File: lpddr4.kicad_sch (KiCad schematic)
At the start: 43 parts, among them U1 MT53E1G32D2NP-046

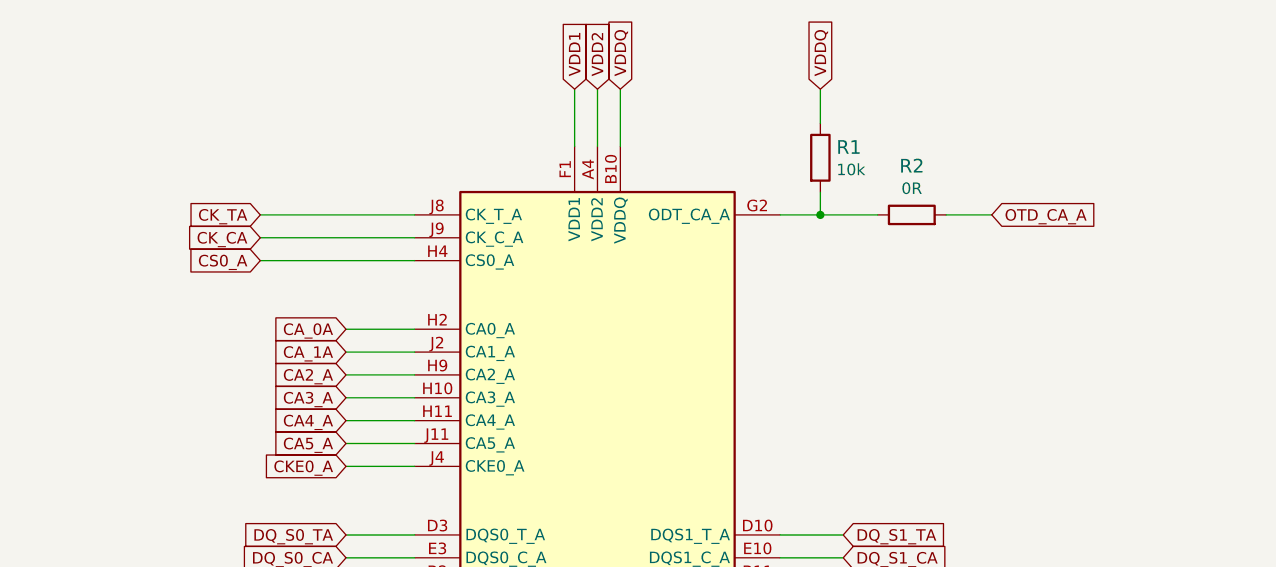
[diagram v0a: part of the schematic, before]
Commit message: Fix net names
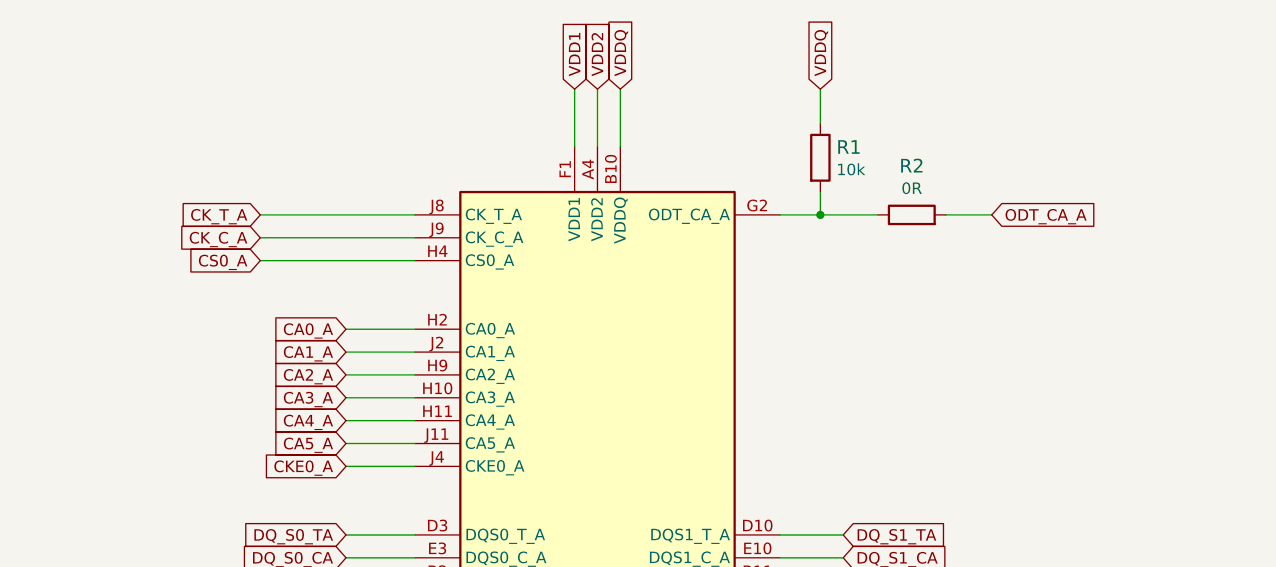
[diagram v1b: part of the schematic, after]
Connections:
- net CA_0A renamed CA0_A
- net CA_1A renamed CA1_A
- net CK_CA renamed CK_C_A
- net CK_TA renamed CK_T_A
- net OTD_CA_A renamed ODT_CA_A

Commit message: Update signage
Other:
- moved on the sheet: C1, C10, C11, C12, C13, C14, C15, C16, C17, C18, C19, C2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

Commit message: [#45231] globlib
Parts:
- C1, C10, C11, C12, C13, C14, C15, C16, C17, C18, C19, C2, C20, C21, C22, C23, C24, C25, C26, C27, C28, C29, C3, C30, C31, C32, C33, C35, C36, C4, C5, C6, C7, C8, C9: footprint lpddr4-testbed-footprints:0201-res -> antmicro-footprints:C_0201; symbol lpddr4-testbed:C_100n_0201 -> antmicroCapacitorsmisc:C_100n_0201
- R1, R3, R4, R5: footprint lpddr4-testbed-footprints:0402-res -> antmicro-footprints:R_0402_1005Metric; symbol lpddr4-testbed:R_10k_0402 -> antmicroResistors0402:R_10k_0402
- R2, R7: footprint lpddr4-testbed-footprints:0402-res -> antmicro-footprints:R_0402_1005Metric; symbol lpddr4-testbed:R_0R_0402 -> antmicroResistors0402:R_0R_0402
- R6: footprint lpddr4-testbed-footprints:0402-res -> antmicro-footprints:R_0402_1005Metric; symbol lpddr4-testbed:R_240R_0402 -> antmicroResistors0402:R_240R_0402
- U1: footprint lpddr4-testbed-footprints:BGA-200_10.0x14.5mm_Layout12x22_P0.80x0.65mm -> antmicro-footprints:BGA-200_10.0x14.5mm_Layout12x22_P0.80x0.65mm; symbol lpddr4-testbed:MT53E1G32D2NP-046 -> antmicroMemory:MT53E1G32D2NP-046

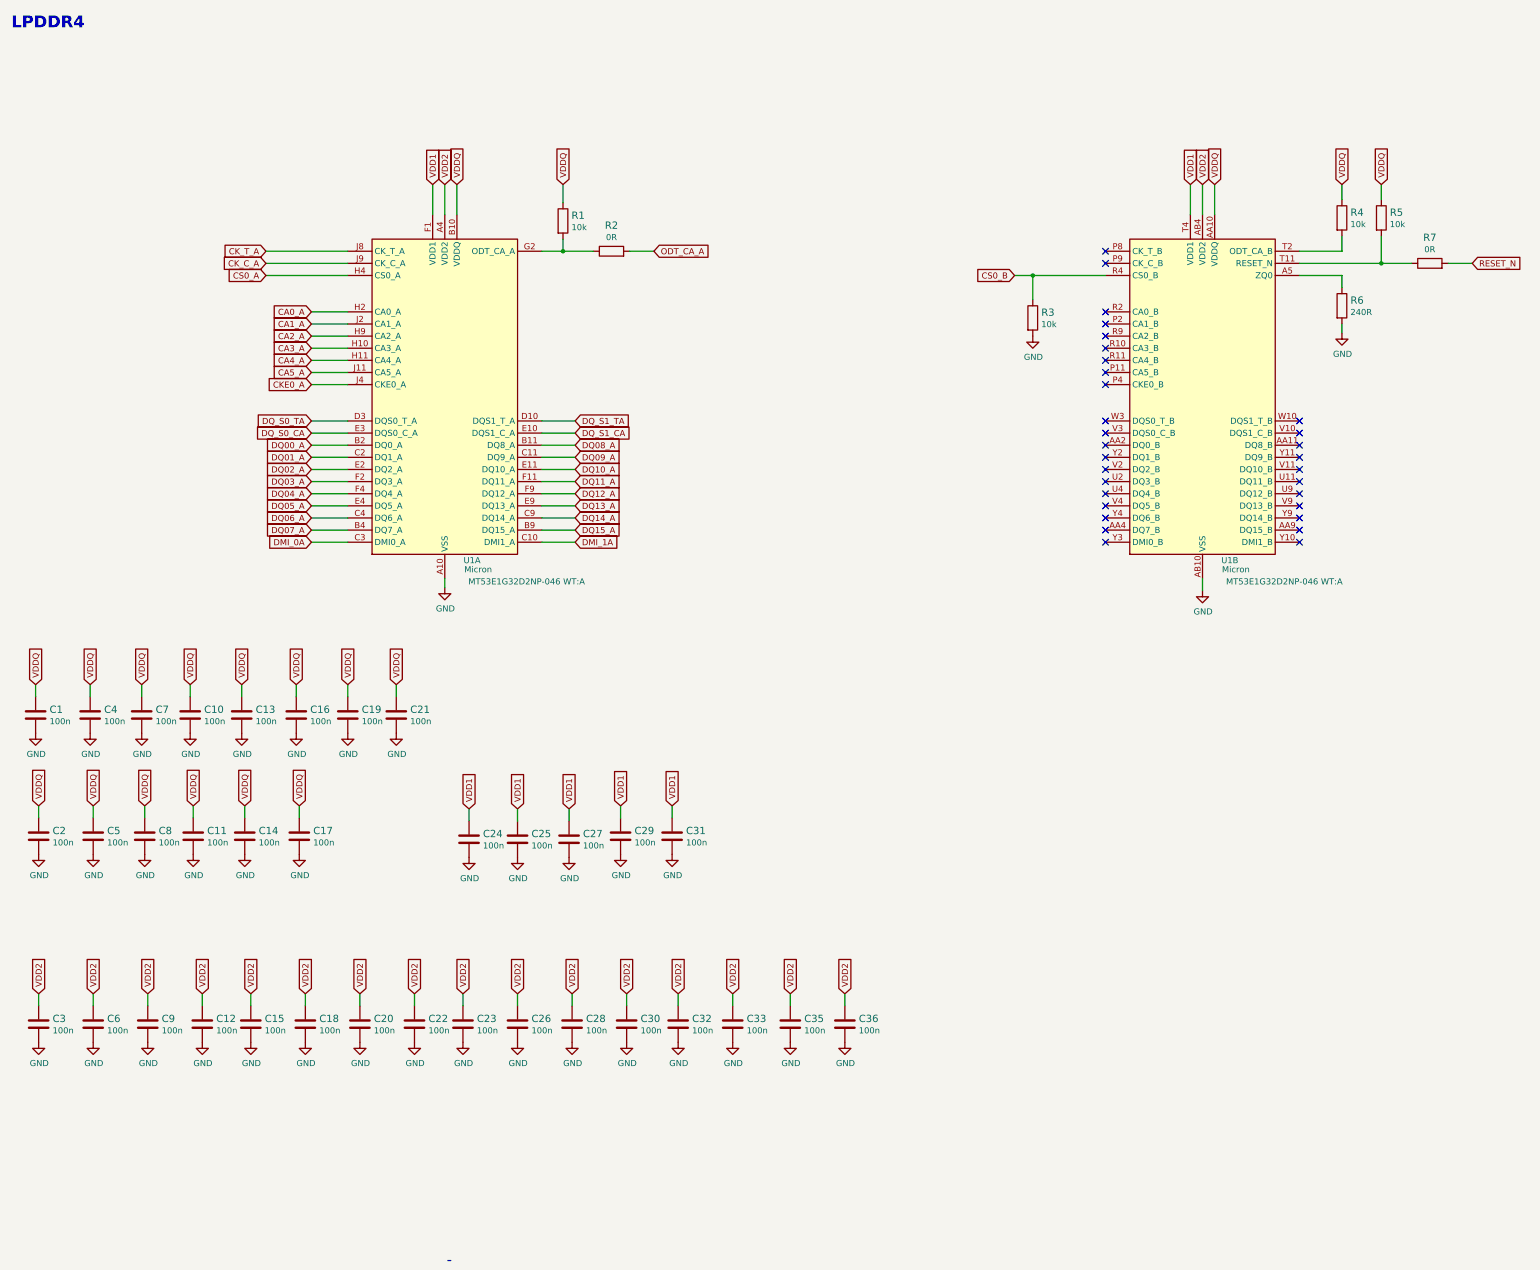
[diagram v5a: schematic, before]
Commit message: Introduce component standardization
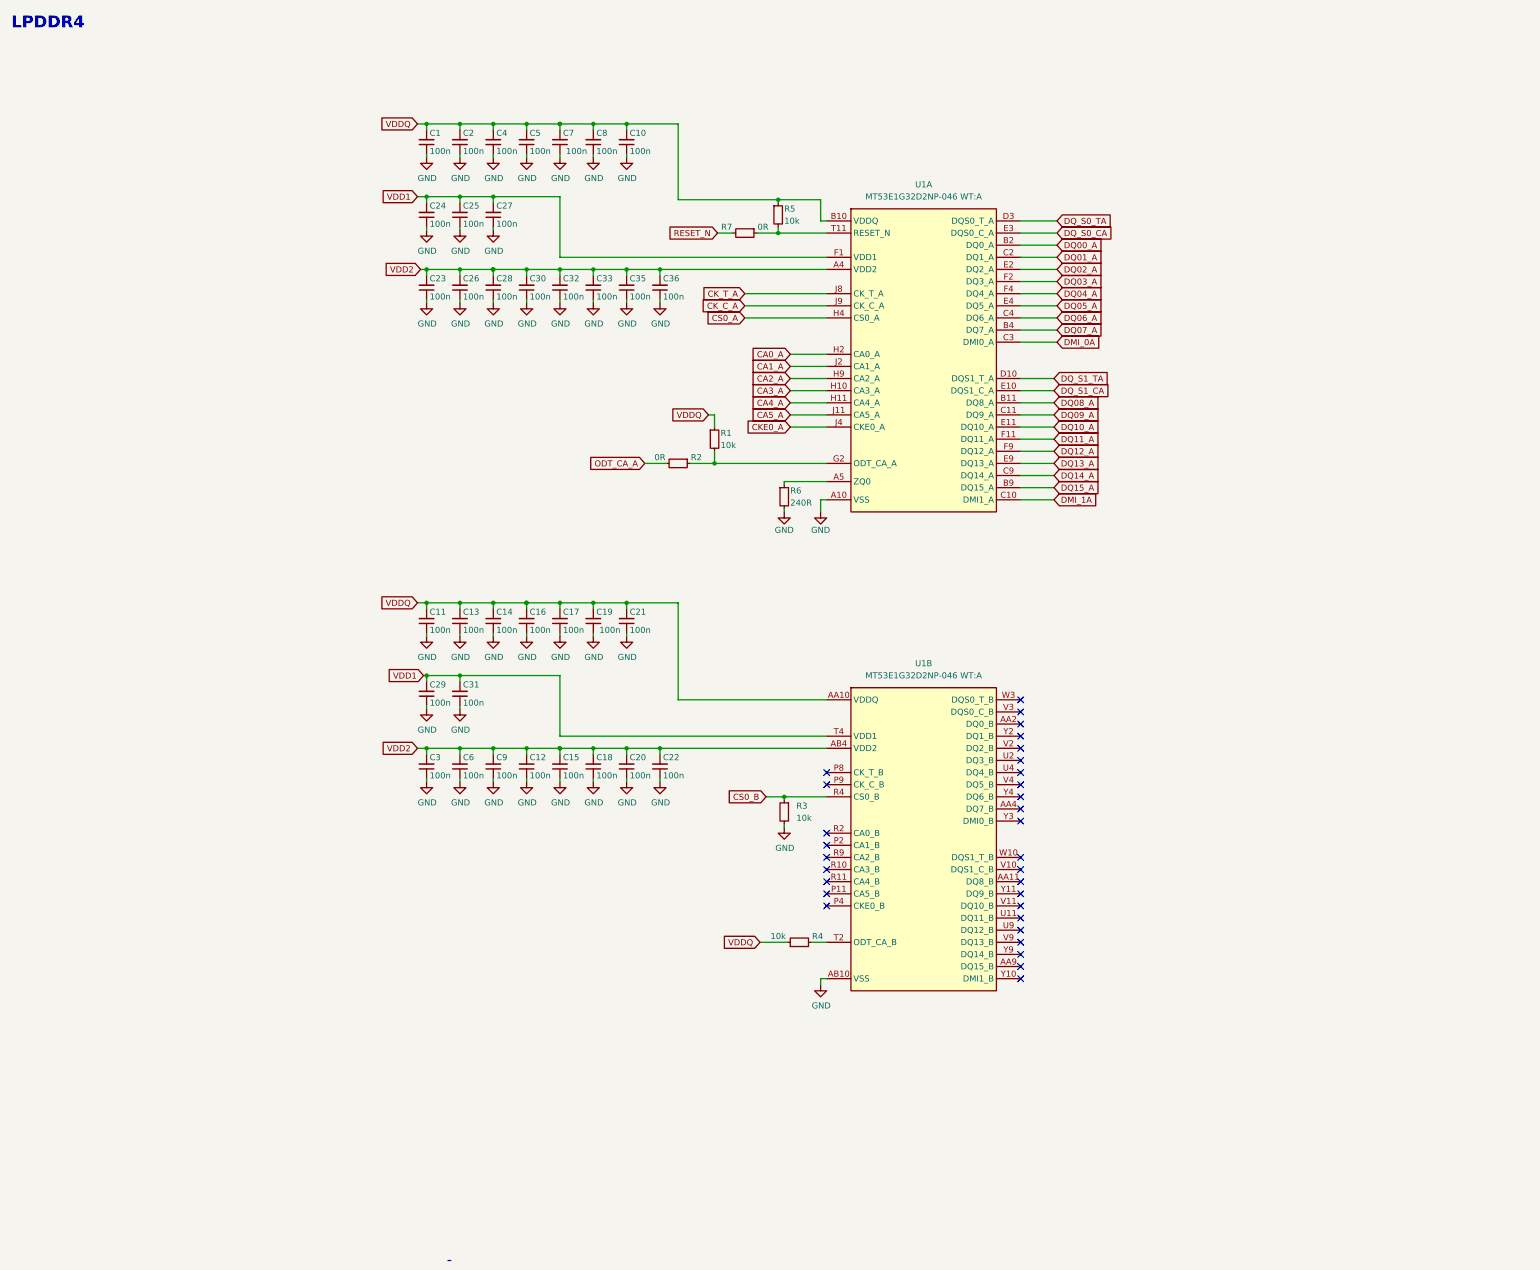
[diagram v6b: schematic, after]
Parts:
- C1, C10, C11, C12, C13, C14, C15, C16, C17, C18, C19, C2, C20, C21, C22, C23, C24, C25, C26, C27, C28, C29, C3, C30, C31, C32, C33, C35, C36, C4, C5, C6, C7, C8, C9: footprint antmicro-footprints:C_0201 -> lpddr4-testbed-footprints:C_0201; symbol antmicroCapacitorsmisc:C_100n_0201 -> lpddr4-testbed:C_100n_0201; Author (none) -> Antmicro; License (none) -> Apache-2.0
- R1, R3, R4, R5: footprint antmicro-footprints:R_0402_1005Metric -> lpddr4-testbed-footprints:R_0402_1005Metric; symbol antmicroResistors0402:R_10k_0402 -> lpddr4-testbed:R_10k_0402; Author (none) -> Antmicro; License (none) -> Apache-2.0; Tolerance (none) -> 1%
- R2, R7: footprint antmicro-footprints:R_0402_1005Metric -> lpddr4-testbed-footprints:R_0402_1005Metric; symbol antmicroResistors0402:R_0R_0402 -> lpddr4-testbed:R_0R_0402; Author (none) -> Antmicro; Current (none) -> 1A; License (none) -> Apache-2.0
- R6: footprint antmicro-footprints:R_0402_1005Metric -> lpddr4-testbed-footprints:R_0402_1005Metric; symbol antmicroResistors0402:R_240R_0402 -> lpddr4-testbed:R_240R_0402; Author (none) -> Antmicro; License (none) -> Apache-2.0; Tolerance (none) -> 1%
- U1: footprint antmicro-footprints:BGA-200_10.0x14.5mm_Layout12x22_P0.80x0.65mm -> lpddr4-testbed-footprints:BGA-200_10.0x14.5mm_Layout12x22_P0.80x0.65mm; symbol antmicroMemory:MT53E1G32D2NP-046 -> lpddr4-testbed:MT53E1G32D2NP-046; Author (none) -> Antmicro; License (none) -> Apache-2.0
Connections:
- net GND: now also C1.1, C10.1, C11.1, C12.1, C13.1, C14.1, C15.1, C16.1, C17.1, C18.1, C19.1, C2.1, C20.1, C21.1, C22.1, C23.1, C24.1, C25.1, C26.1, C27.1, C28.1, C29.1, C3.1, C30.1, C31.1, C32.1, C33.1, C35.1, C36.1, C4.1, C5.1, C6.1, C7.1, C8.1, C9.1; no longer C1.2, C10.2, C11.2, C12.2, C13.2, C14.2, C15.2, C16.2, C17.2, C18.2, C19.2, C2.2, C20.2, C21.2, C22.2, C23.2, C24.2, C25.2, C26.2, C27.2, C28.2, C29.2, C3.2, C30.2, C31.2, C32.2, C33.2, C35.2, C36.2, C4.2, C5.2, C6.2, C7.2, C8.2, C9.2
- net VDD1: now also C24.2, C25.2, C27.2, C29.2, C31.2; no longer C24.1, C25.1, C27.1, C29.1, C31.1
- net VDD2: now also C12.2, C15.2, C18.2, C20.2, C22.2, C23.2, C26.2, C28.2, C3.2, C30.2, C32.2, C33.2, C35.2, C36.2, C6.2, C9.2; no longer C12.1, C15.1, C18.1, C20.1, C22.1, C23.1, C26.1, C28.1, C3.1, C30.1, C32.1, C33.1, C35.1, C36.1, C6.1, C9.1
- net VDDQ: now also C1.2, C10.2, C11.2, C13.2, C14.2, C16.2, C17.2, C19.2, C2.2, C21.2, C4.2, C5.2, C7.2, C8.2; no longer C1.1, C10.1, C11.1, C13.1, C14.1, C16.1, C17.1, C19.1, C2.1, C21.1, C4.1, C5.1, C7.1, C8.1
- net at R5.2, R7.1: now also U1.T11 (RESET_N); no longer U1.T11 (RESET_N)
- net at R6.1: now also U1.A5 (ZQ0); no longer U1.A5 (ZQ0)
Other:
- title: (none) -> LPDDR4 testbed
- moved on the sheet: C1, C10, C11, C12, C13, C14, C15, C16, C17, C18, C19, C2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

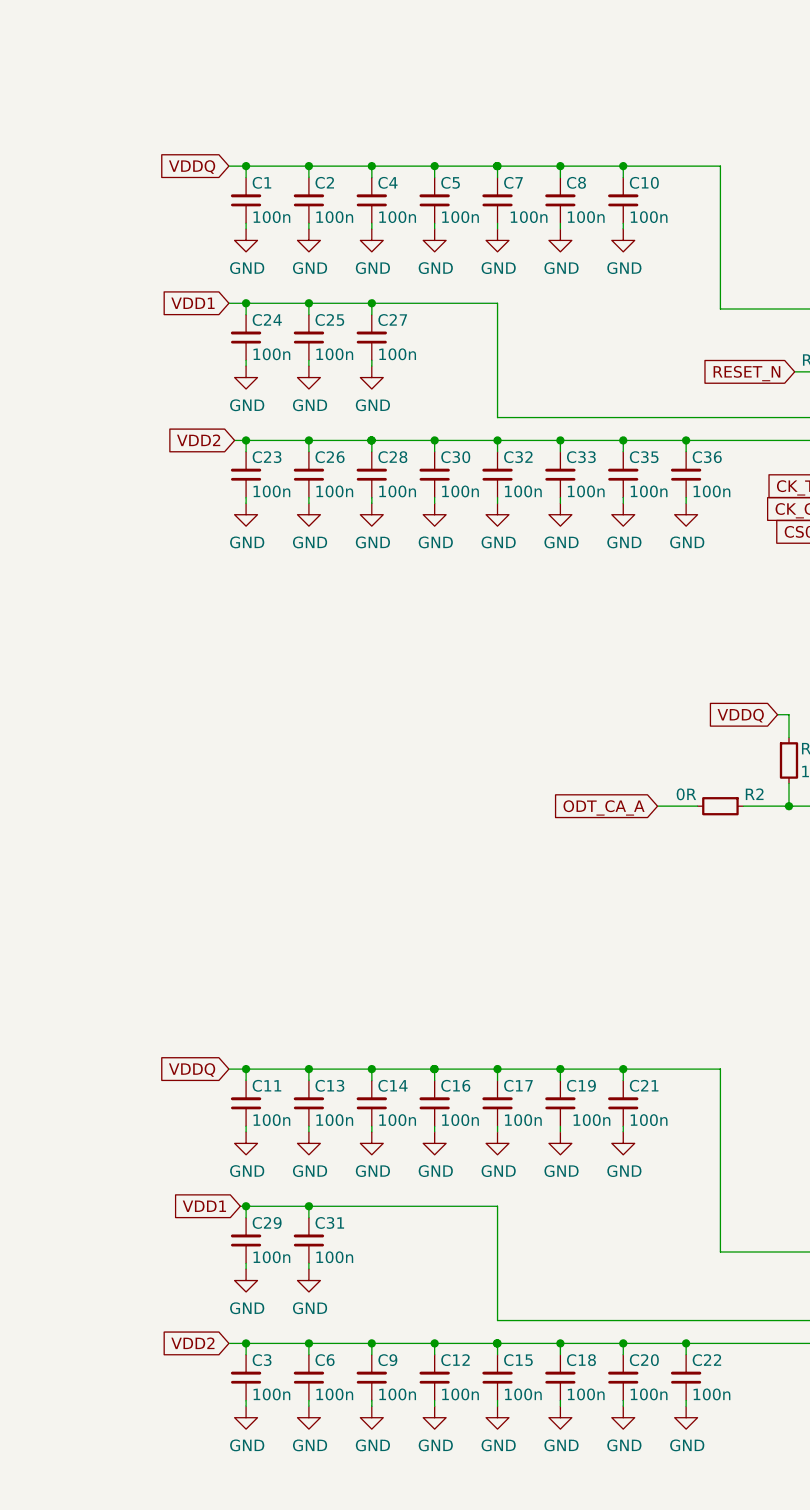
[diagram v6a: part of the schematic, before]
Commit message: [#56947] Correct component references
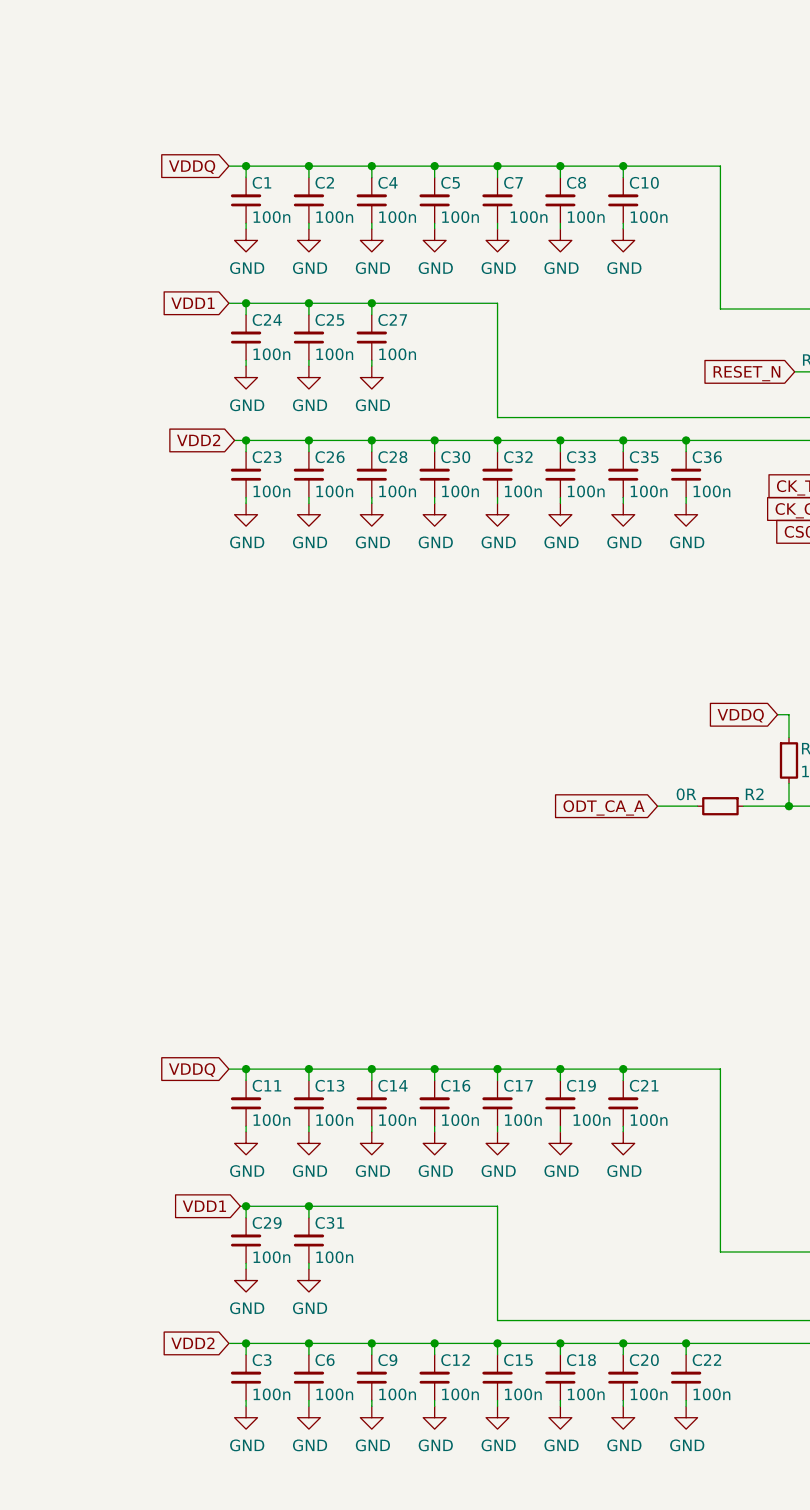
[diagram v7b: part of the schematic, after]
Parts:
- C1, C10, C11, C12, C13, C14, C15, C16, C17, C18, C19, C2, C20, C21, C22, C23, C24, C25, C26, C27, C28, C29, C3, C30, C31, C32, C33, C35, C36, C4, C5, C6, C7, C8, C9: footprint lpddr4-testbed-footprints:C_0201 -> antmicro-footprints:C_0201; symbol lpddr4-testbed:C_100n_0201 -> antmicroCapacitorsmisc:C_100n_0201
- R1, R3, R4, R5: footprint lpddr4-testbed-footprints:R_0402_1005Metric -> antmicro-footprints:R_0402_1005Metric; symbol lpddr4-testbed:R_10k_0402 -> antmicroResistors0402:R_10k_0402
- R2, R7: footprint lpddr4-testbed-footprints:R_0402_1005Metric -> antmicro-footprints:R_0402_1005Metric; symbol lpddr4-testbed:R_0R_0402 -> antmicroResistors0402:R_0R_0402
- R6: footprint lpddr4-testbed-footprints:R_0402_1005Metric -> antmicro-footprints:R_0402_1005Metric; symbol lpddr4-testbed:R_240R_0402 -> antmicroResistors0402:R_240R_0402
- U1: footprint lpddr4-testbed-footprints:BGA-200_10.0x14.5mm_Layout12x22_P0.80x0.65mm -> antmicro-footprints:BGA-200_10.0x14.5mm_Layout12x22_P0.80x0.65mm; symbol lpddr4-testbed:MT53E1G32D2NP-046 -> antmicroMemory:MT53E1G32D2NP-046

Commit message: [#56947] Fix missing highlights in OHP
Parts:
- U1: Manufacturer Micron -> Micron Technology
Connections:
- net at U1.AA1 (DNU): now also U1.AA12 (DNU), U1.AB1 (DNU), U1.AB11 (DNU), U1.AB12 (DNU), U1.AB2 (DNU)
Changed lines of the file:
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@@
       (effects (font (size 1.27 1.27) (thickness 0.15)) (justify left bottom) hide)
     )
-    (property "Datasheet" "" (at 195.58 96.52 0)
-      (effects (font (size 1.27 1.27) (thickness 0.15)) (justify left bottom) hide)
-    )
-    (property "Manufacturer" "Micron" (at 218.44 58.42 0)
+    (property "Datasheet" "https://www.micron.com/products/dram/lpdram/part-catalog/mt53e1g32d2np-046-wt" (at 195.58 96.52 0)
+      (effects (font (size 1.27 1.27) (thickness 0.15)) (justify left bottom) hide)
+    )
+    (property "Manufacturer" "Micron Technology" (at 218.44 58.42 0)
       (effects (font (size 1.27 1.27) (thickness 0.15)) (justify left bottom) hide)
     )
@@
     )
   )
-  (symbol (lib_name "MT53E1G32D2NP-046_1") (lib_id "antmicroMemory:MT53E1G32D2NP-046") (at 198.12 166.37 0) (unit 2)
+  (symbol (lib_id "antmicroMemory:MT53E1G32D2NP-046") (at 198.12 166.37 0) (unit 2)
     (in_bom yes) (on_board yes) (dnp no) (fields_autoplaced)
     (property "Reference" "U1" (at 218.44 158.75 0)
@@
       (effects (font (size 1.27 1.27) (thickness 0.15)) (justify left bottom) hide)
     )
-    (property "Datasheet" "" (at 195.58 196.85 0)
-      (effects (font (size 1.27 1.27) (thickness 0.15)) (justify left bottom) hide)
-    )
-    (property "Manufacturer" "Micron" (at 220.4594 242.57 0)
-      (effects (font (size 1.27 1.27) (thickness 0.15)) (justify left bottom) hide)
-    )
+    (property "Datasheet" "https://www.micron.com/products/dram/lpdram/part-catalog/mt53e1g32d2np-046-wt" (at 195.58 196.85 0)
+      (effects (font (size 1.27 1.27) (thickness 0.15)) (justify left bottom) hide)
+    )
+    (property "Manufacturer" "Micron Technology" (at 220.4594 242.57 0)
+      (effects (font (size 1.27 1.27) (thickness 0.15)) (justify left bottom) hide)
+    )
